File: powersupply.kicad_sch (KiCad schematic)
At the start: 17 parts, among them U1 BP2525

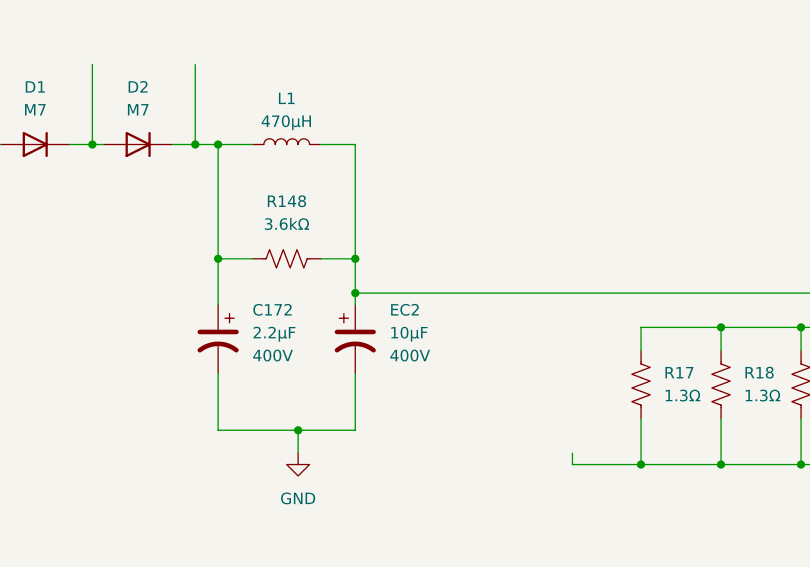
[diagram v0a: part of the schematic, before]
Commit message: Looking quite accurate. Time to fix connector foots.
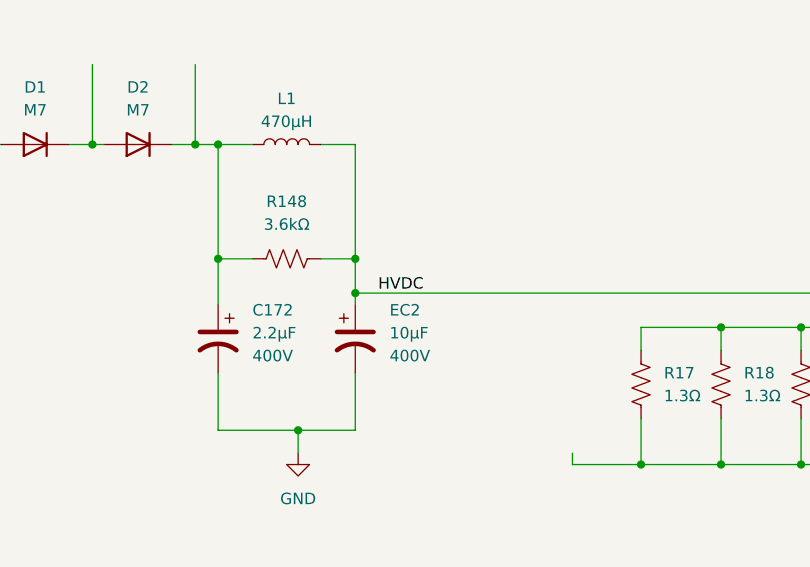
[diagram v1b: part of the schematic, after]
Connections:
- net HVDC: now reaches EC2.1, L1.2, R148.2, U1.4 (DRAIN)
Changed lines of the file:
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@@
+		)
+	)
+	(label "HVDC"
+		(at 86.36 73.66 0)
+		(effects
+			(font
+				(size 1.27 1.27)
+			)
+			(justify left bottom)
 		)
 	)

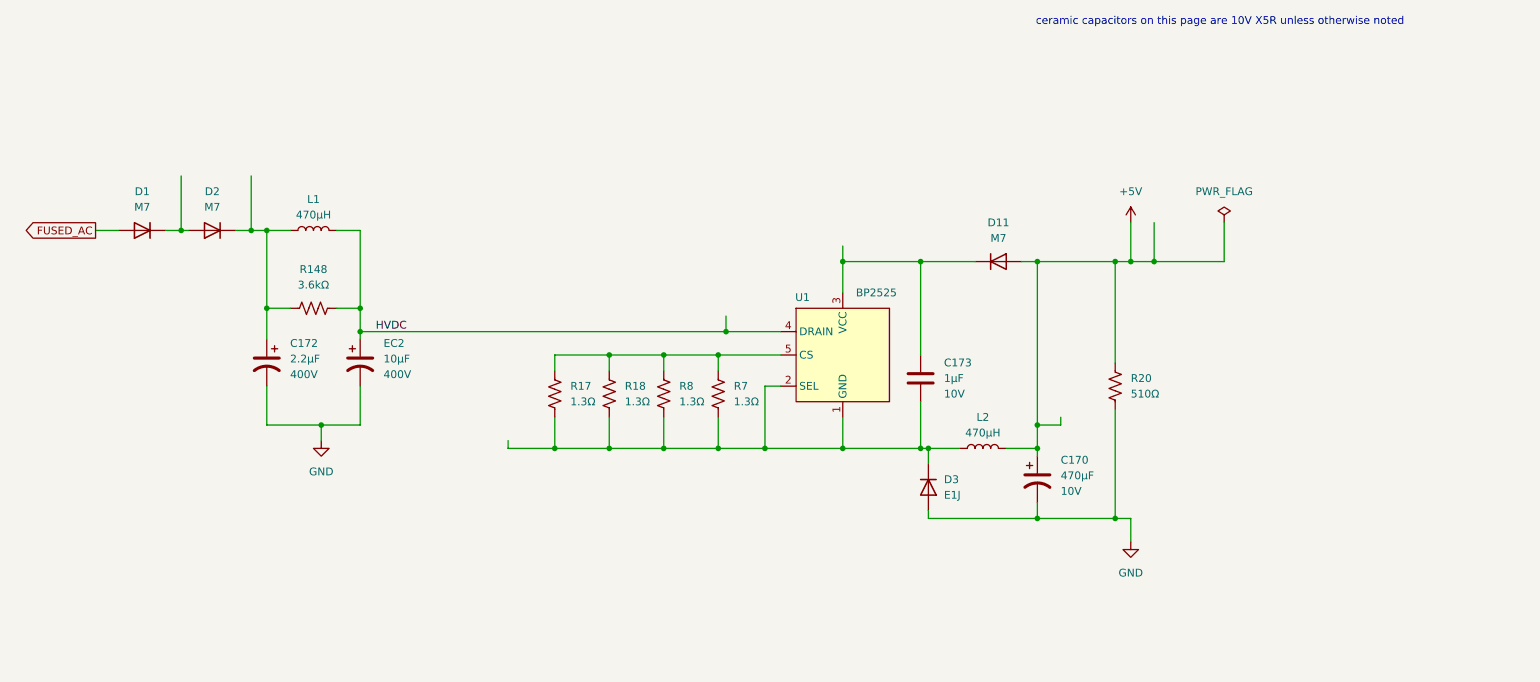
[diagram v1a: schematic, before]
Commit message: Cleaned schematic. Still have silk and fab to do. Also have not fixed F1. Have decided I may not fix F1.
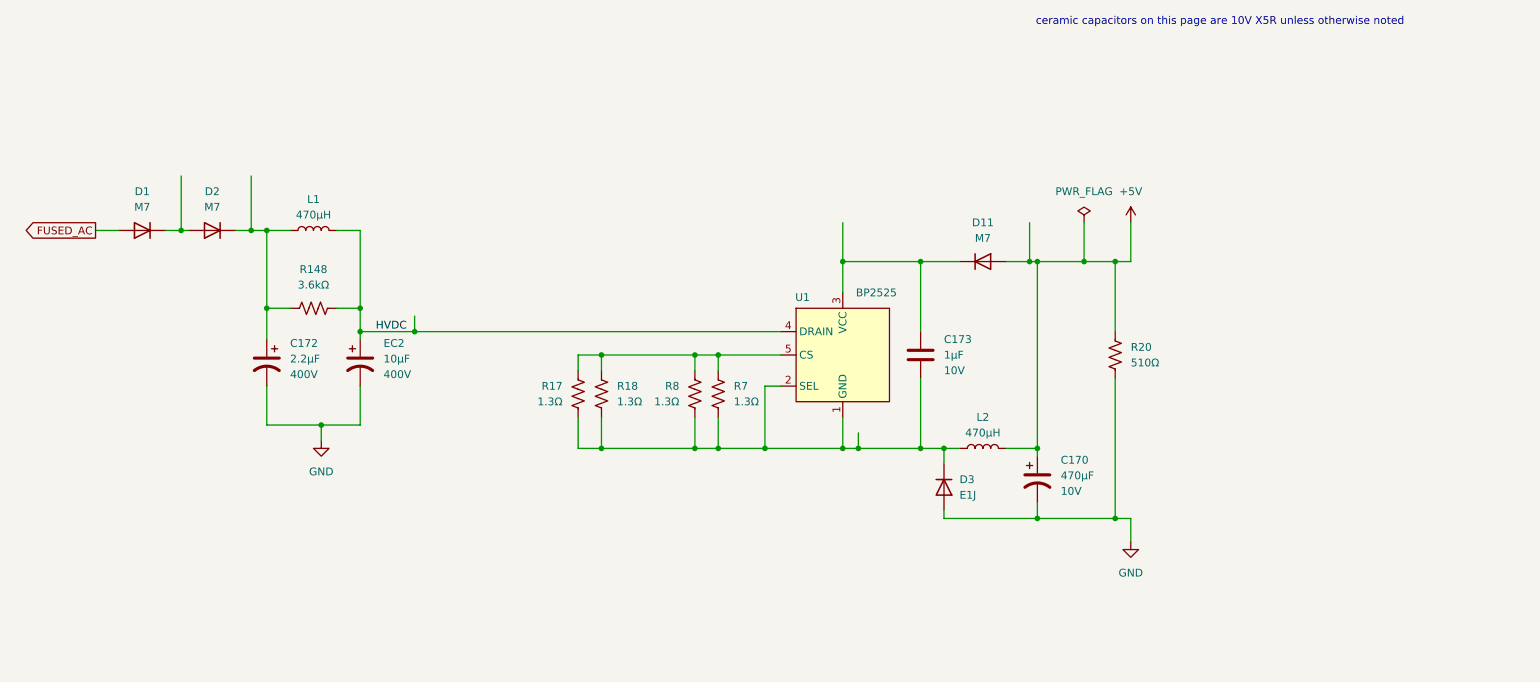
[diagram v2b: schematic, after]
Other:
- title: (none) -> T smart switched power outlet
- moved on the sheet: C173, D11, D3, R17, R18, R20, R8

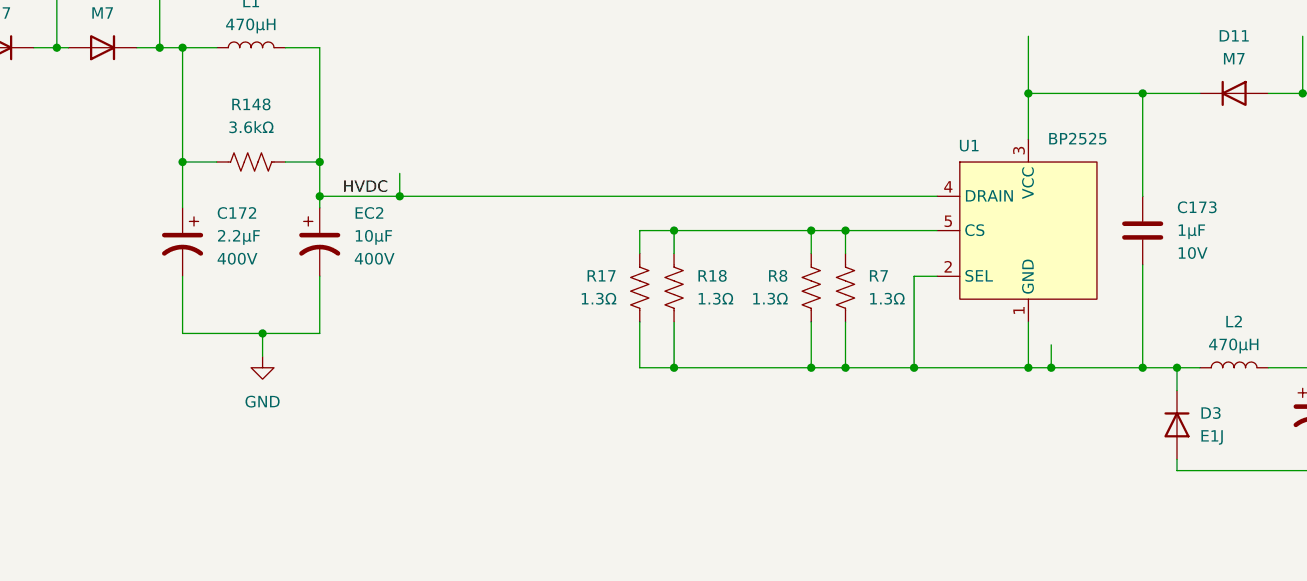
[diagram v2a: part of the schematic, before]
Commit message: Added description of microcontroller subboard to schematic.
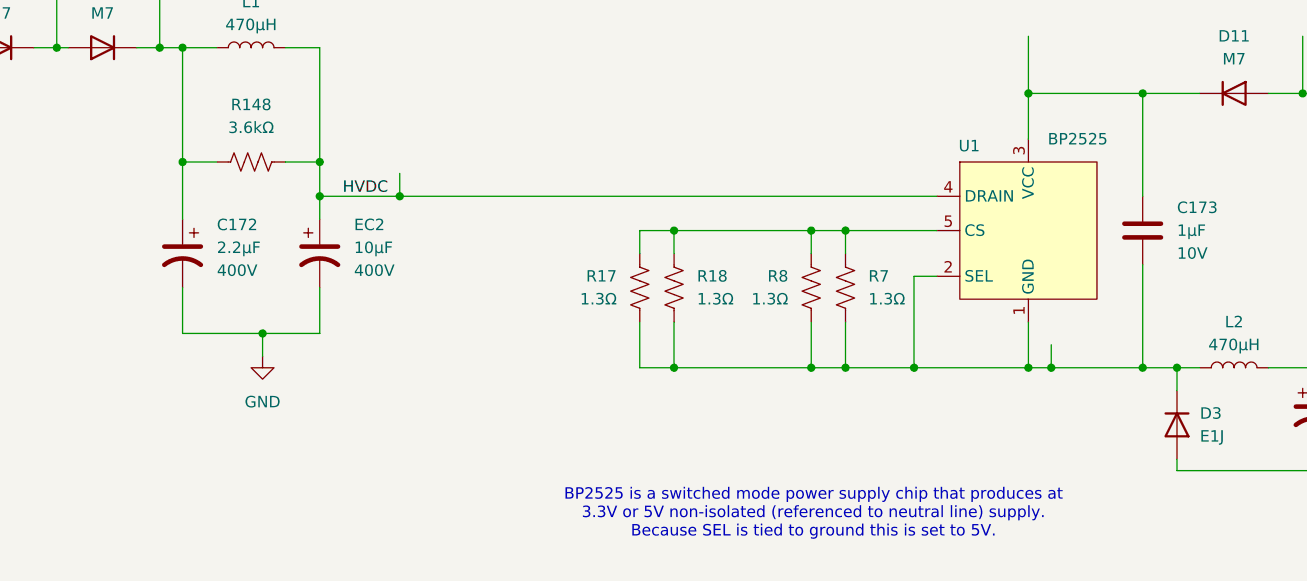
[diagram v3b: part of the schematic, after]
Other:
- note added: "BP2525 is a switched mode power supply chip that produces at 3.3V or 5V non-isolated (referenced to neutral line) supply. Because SEL is tied to ground this is set to 5V."
- moved on the sheet: C172, EC2
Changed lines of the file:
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@@
+		)
+	)
+	(text "BP2525 is a switched mode power supply chip that produces at\n3.3V or 5V non-isolated (referenced to neutral line) supply.\nBecause SEL is tied to ground this is set to 5V."
+		(exclude_from_sim no)
+		(at 138.684 108.966 0)
+		(effects
+			(font
+				(size 1.27 1.27)
+			)
 		)
 	)
@@
 	(wire
 		(pts
-			(xy 83.82 73.66) (xy 83.82 74.93)
+			(xy 83.82 73.66) (xy 83.82 76.2)
 		)
 		(stroke
@@
 	(wire
 		(pts
-			(xy 83.82 82.55) (xy 83.82 88.9)
+			(xy 83.82 83.82) (xy 83.82 88.9)
 		)
 		(stroke
@@
 	(wire
 		(pts
-			(xy 68.58 69.85) (xy 68.58 74.93)
-		)
-		(stroke
-			(width 0)
-			(type default)
-		)
-	)
-	(wire
-		(pts
-			(xy 68.58 88.9) (xy 68.58 82.55)
+			(xy 68.58 69.85) (xy 68.58 76.2)
+		)
+		(stroke
+			(width 0)
+			(type default)
+		)
+	)
+	(wire
+		(pts
+			(xy 68.58 88.9) (xy 68.58 83.82)
 		)
 		(stroke
@@
 			)
 		)
-		(property "Datasheet" "~"
+		(property "Datasheet" "https://mm.digikey.com/Volume0/opasdata/d220001/medias/docus/6778/5399_E1J%20SOD-123FL.PDF"
 			(at 179.07 99.06 0)
 			(effects
@@
 	(symbol
 		(lib_id "Device:C_Polarized_US")
-		(at 68.58 78.74 0)
+		(at 68.58 80.01 0)
 		(mirror y)
 		(unit 1)
@@
 		(fields_autoplaced yes)
 		(property "Reference" "C172"
-			(at 72.39 75.5649 0)
+			(at 72.39 76.8349 0)
 			(effects
 				(font
@@
 		)
 		(property "Value" "2.2µF"
-			(at 72.39 78.1049 0)
+			(at 72.39 79.3749 0)
 			(effects
 				(font
@@
 		)
 		(property "Footprint" "Capacitor_THT:CP_Radial_D6.3mm_P2.50mm"
-			(at 68.58 78.74 0)
+			(at 68.58 80.01 0)
 			(effects
 				(font
@@
 		)
 		(property "Datasheet" "~"
-			(at 68.58 78.74 0)
+			(at 68.58 80.01 0)
 			(effects
 				(font
@@
 		)
 		(property "Description" "Polarized capacitor, US symbol"
-			(at 68.58 78.74 0)
+			(at 68.58 80.01 0)
 			(effects
 				(font
@@
 		)
 		(property "Voltage" "400V"
-			(at 72.39 80.6449 0)
+			(at 72.39 81.9149 0)
 			(effects
 				(font
@@
 	(symbol
 		(lib_id "Device:C_Polarized_US")
-		(at 83.82 78.74 0)
+		(at 83.82 80.01 0)
 		(unit 1)
 		(exclude_from_sim no)
@@
 		(fields_autoplaced yes)
 		(property "Reference" "EC2"
-			(at 87.63 75.5649 0)
+			(at 87.63 76.8349 0)
 			(effects
 				(font
@@
 		)
 		(property "Value" "10µF"
-			(at 87.63 78.1049 0)
+			(at 87.63 79.3749 0)
 			(effects
 				(font
@@
 		)
 		(property "Footprint" "Capacitor_THT:CP_Radial_D8.0mm_P3.50mm"
-			(at 83.82 78.74 0)
+			(at 83.82 80.01 0)
 			(effects
 				(font
@@
 		)
 		(property "Datasheet" "~"
-			(at 83.82 78.74 0)
+			(at 83.82 80.01 0)
 			(effects
 				(font
@@
 		)
 		(property "Description" "Polarized capacitor, US symbol"
-			(at 83.82 78.74 0)
+			(at 83.82 80.01 0)
 			(effects
 				(font
@@
 		)
 		(property "Voltage" "400V"
-			(at 87.63 80.6449 0)
-			(effects
-				(font
+			(at 87.63 81.9149 0)
+			(effects
+				(font

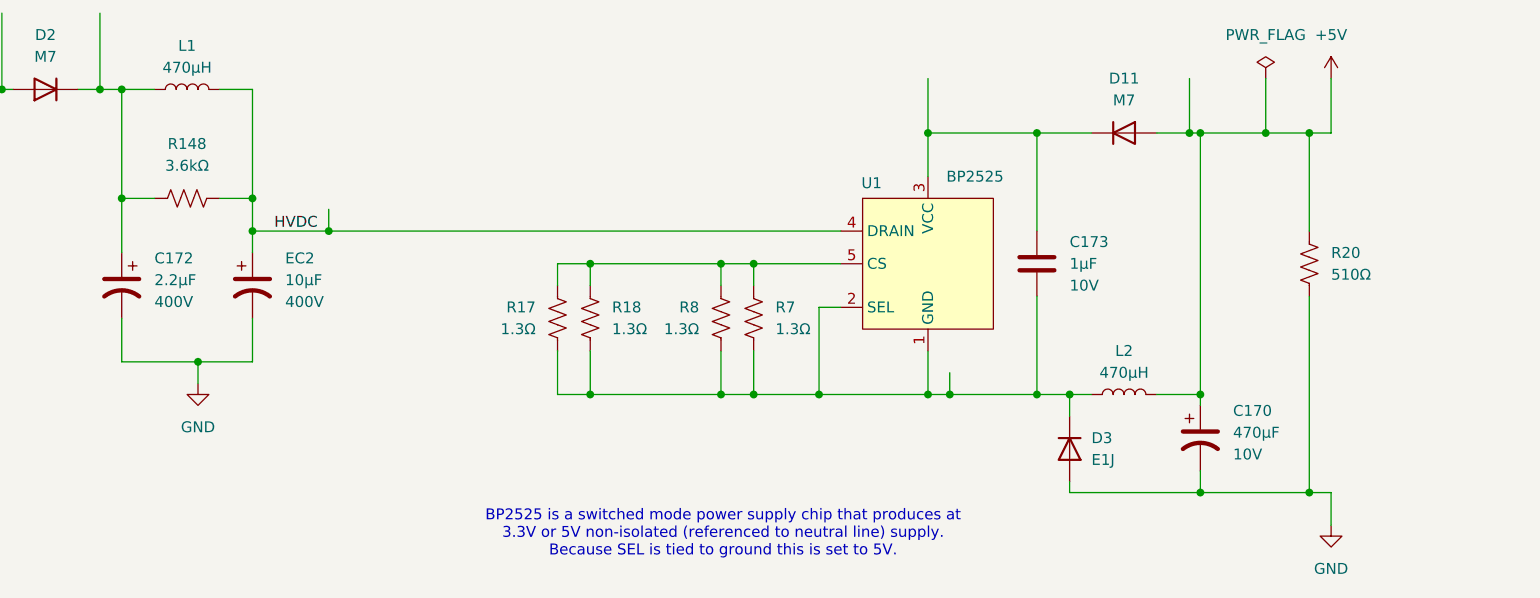
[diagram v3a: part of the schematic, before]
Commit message: Updating project to describe itself better.
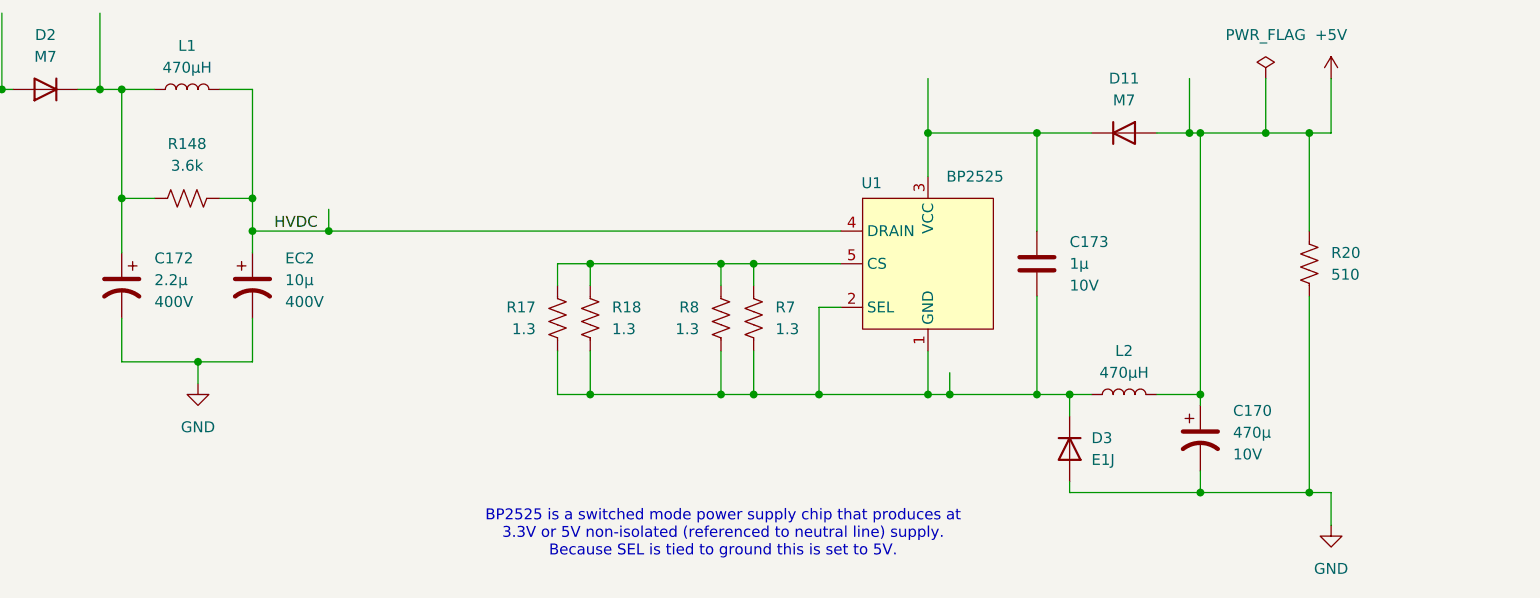
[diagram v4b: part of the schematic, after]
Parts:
- C170: value 470µF -> 470µ
- C172: value 2.2µF -> 2.2µ
- C173: value 1µF -> 1µ
- EC2: value 10µF -> 10µ
- R148: value 3.6kΩ -> 3.6k
- R17, R18, R7, R8: value 1.3Ω -> 1.3
- R20: value 510Ω -> 510
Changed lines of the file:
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@@
 			)
 		)
-		(property "Value" "1.3Ω"
+		(property "Value" "1.3"
 			(at 125.73 85.0899 0)
 			(effects
@@
 			)
 		)
-		(property "Value" "470µF"
+		(property "Value" "470µ"
 			(at 198.12 97.1549 0)
 			(effects
@@
 			)
 		)
-		(property "Value" "1.3Ω"
+		(property "Value" "1.3"
 			(at 144.78 85.0899 0)
 			(effects
@@
 			)
 		)
-		(property "Value" "3.6kΩ"
+		(property "Value" "3.6k"
 			(at 76.2 66.04 90)
 			(effects
@@
 			)
 		)
-		(property "Value" "1µF"
+		(property "Value" "1µ"
 			(at 179.07 77.4699 0)
 			(effects
@@
 			)
 		)
-		(property "Value" "1.3Ω"
+		(property "Value" "1.3"
 			(at 116.84 85.0899 0)
 			(effects
@@
 			)
 		)
-		(property "Value" "2.2µF"
+		(property "Value" "2.2µ"
 			(at 72.39 79.3749 0)
 			(effects
@@
 			)
 		)
-		(property "Value" "510Ω"
+		(property "Value" "510"
 			(at 209.55 78.7399 0)
 			(effects
@@
 			)
 		)
-		(property "Value" "10µF"
+		(property "Value" "10µ"
 			(at 87.63 79.3749 0)
 			(effects
@@
 			)
 		)
-		(property "Value" "1.3Ω"
+		(property "Value" "1.3"
 			(at 135.89 85.0899 0)
 			(effects

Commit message: Updated README to be more detailed. Updated schematic to pass checks and regenerated PDF. Added a few comments. Updated pcb from schematic changes.
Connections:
- net U1_GND: now reaches C173.2, D3.1 (K), L2.1, R17.1, R18.1, R7.1, R8.1, U1.1 (GND), U1.2 (SEL)
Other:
- note added: "M7 diodes are similar in specification to 1N4007 but are in surface mount packages."
- note added: "U1 produces a regulated voltage output at the right side of L2 referenced to system ground even though it does not directly receive system ground. It must rely on a calculated relationship between U1_GND and GND. The datasheet seems to indicate that current sensing is part of this."
- note added: "U1_GND is not the same as system ground."
- moved on the sheet: C170, D3, L2, R20
